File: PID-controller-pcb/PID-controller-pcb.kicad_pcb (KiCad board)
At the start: 2 copper layers, 165.4 x 86 mm, 12 parts, among them SW1 PinHeader_1x03_P2.54mm_Vertic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

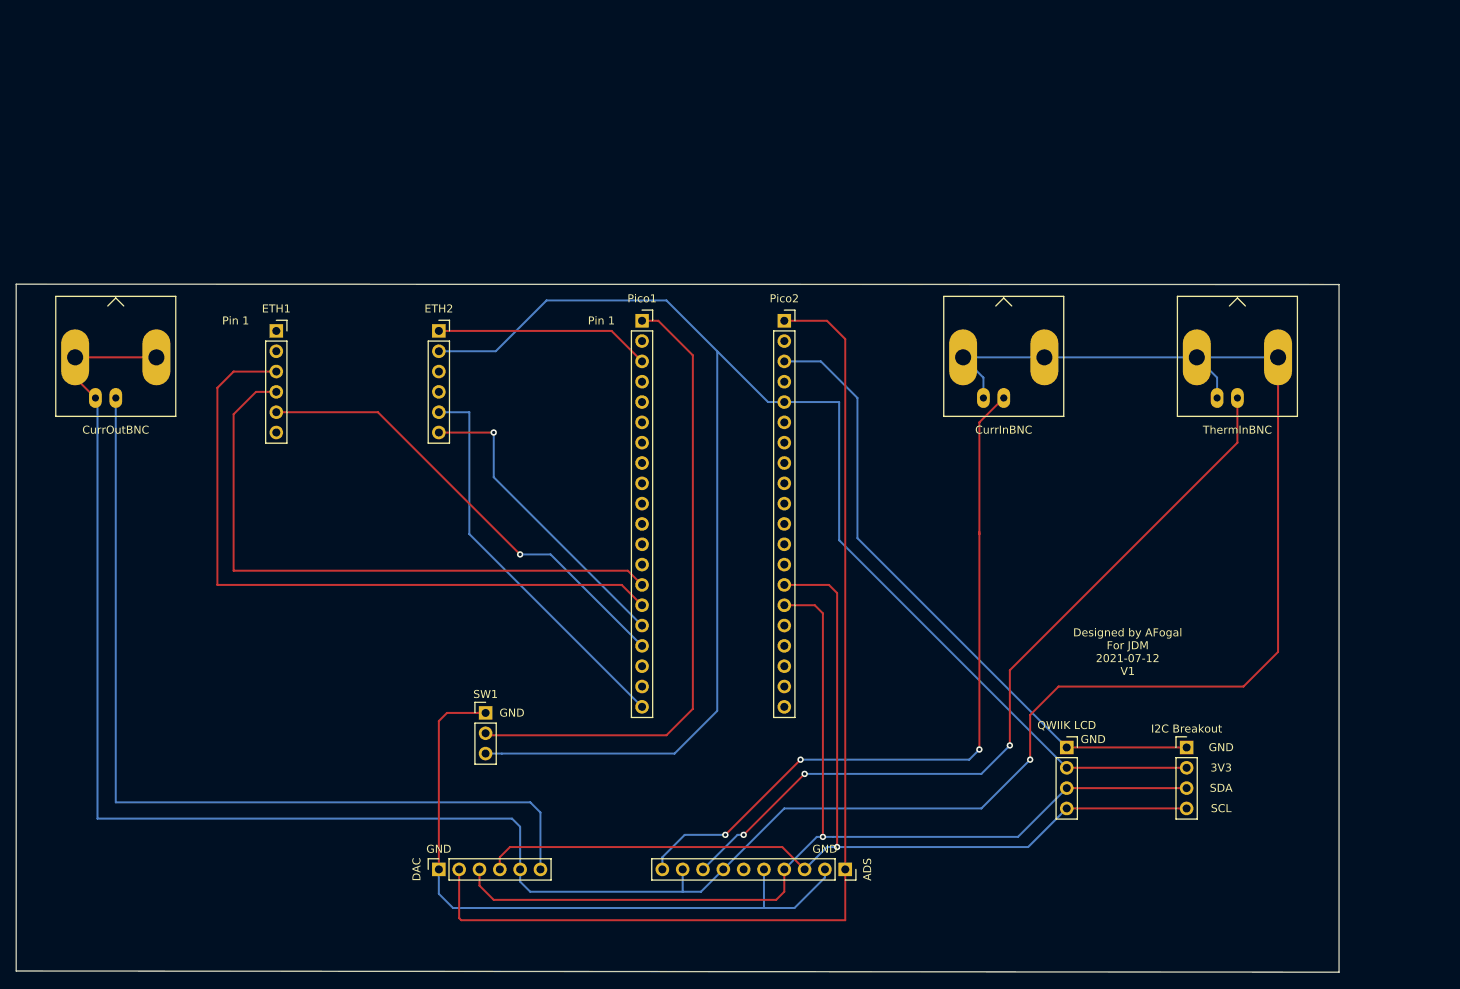
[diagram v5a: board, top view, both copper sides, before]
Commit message: added beagle spy breakout for spi and i2c, didnt route pins 4 or 6 (used for powering device) as we do not want 5V power for spi or i2c
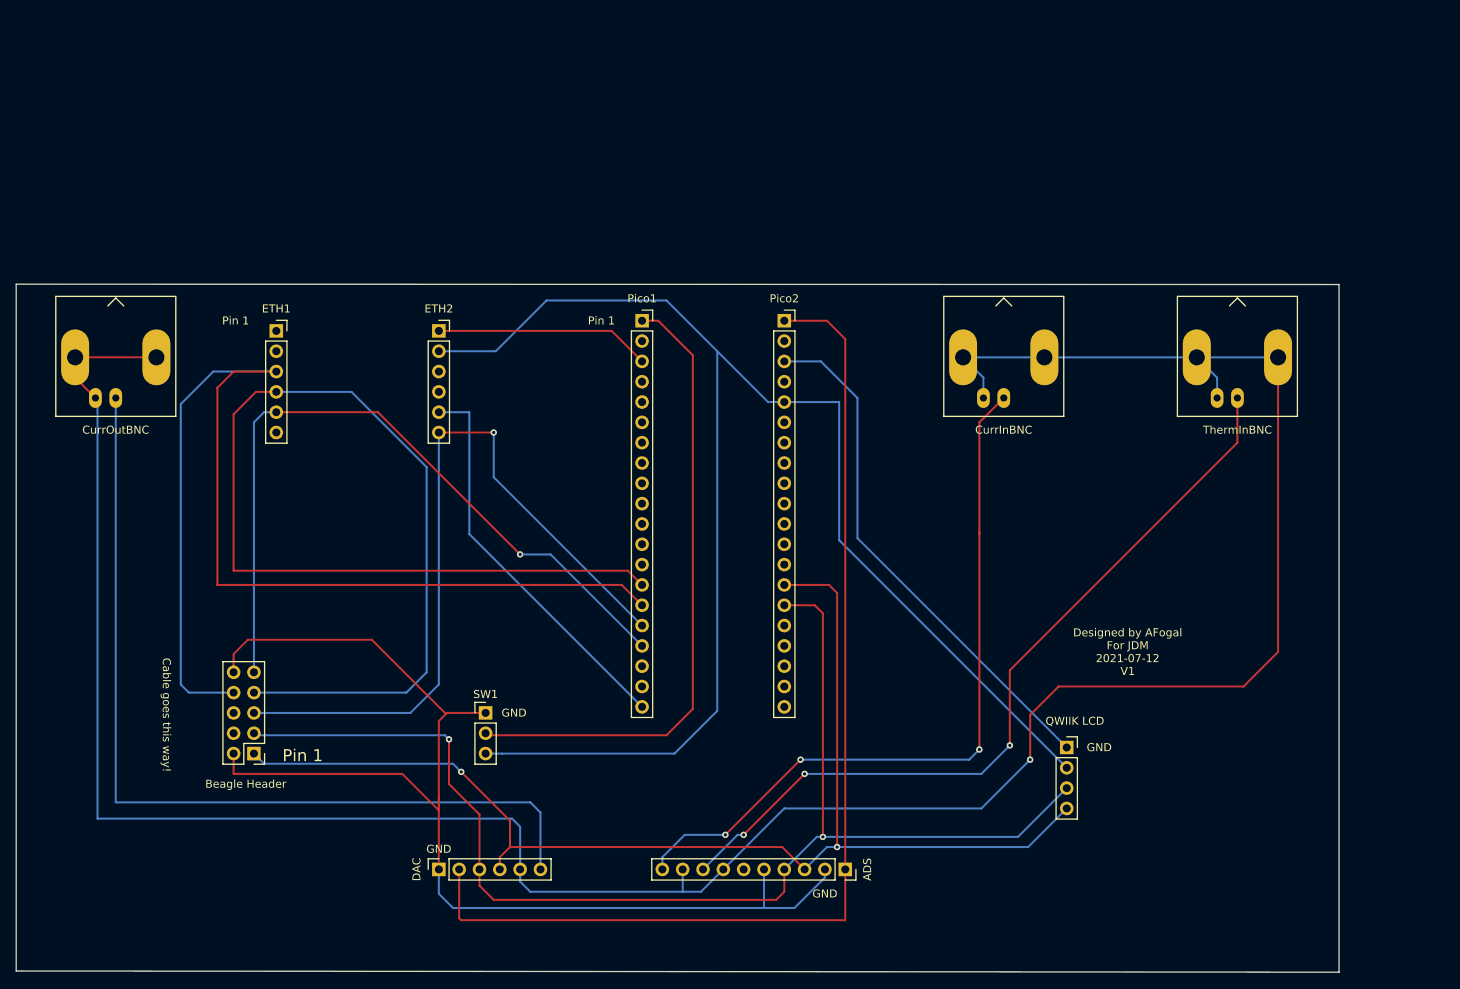
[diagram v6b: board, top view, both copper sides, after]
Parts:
- removed I2C Breakout: PinHeader_1x04_P2.54mm_Vertical, Connector_PinHeader_2.54mm:PinHeader_1x04_P2.54mm_Vertical
- added Beagle Header: PinHeader_2x05_P2.54mm_Vertical, Connector_PinHeader_2.54mm:PinHeader_2x05_P2.54mm_Vertical, F.Cu at (133.1, 103.6)
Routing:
- net (no net): track 1822.1 -> 2126.1 mm, vias 11 -> 13
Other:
- board text added: "Cable goes this way!"
- board text removed: "3V3"
- board text removed: "SCL"
- board text removed: "SDA"

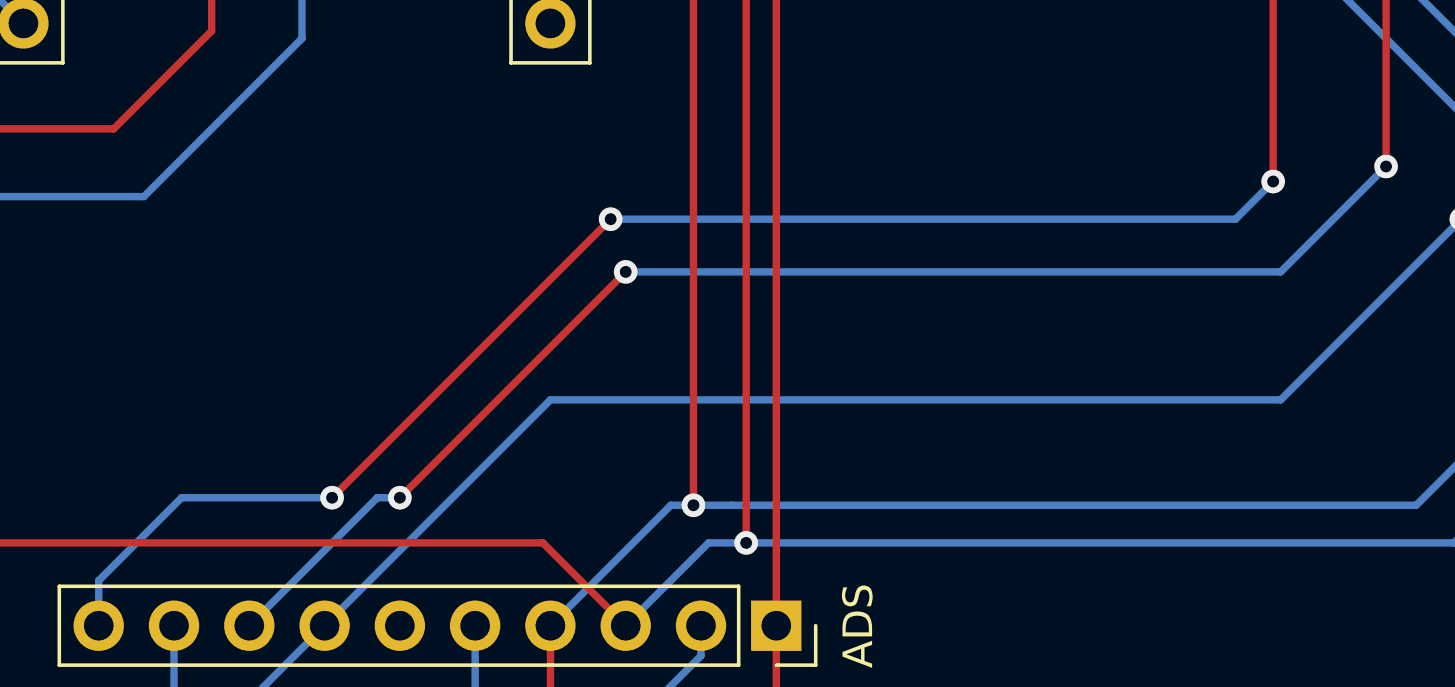
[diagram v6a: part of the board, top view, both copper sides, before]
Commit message: slightly simplified board traces
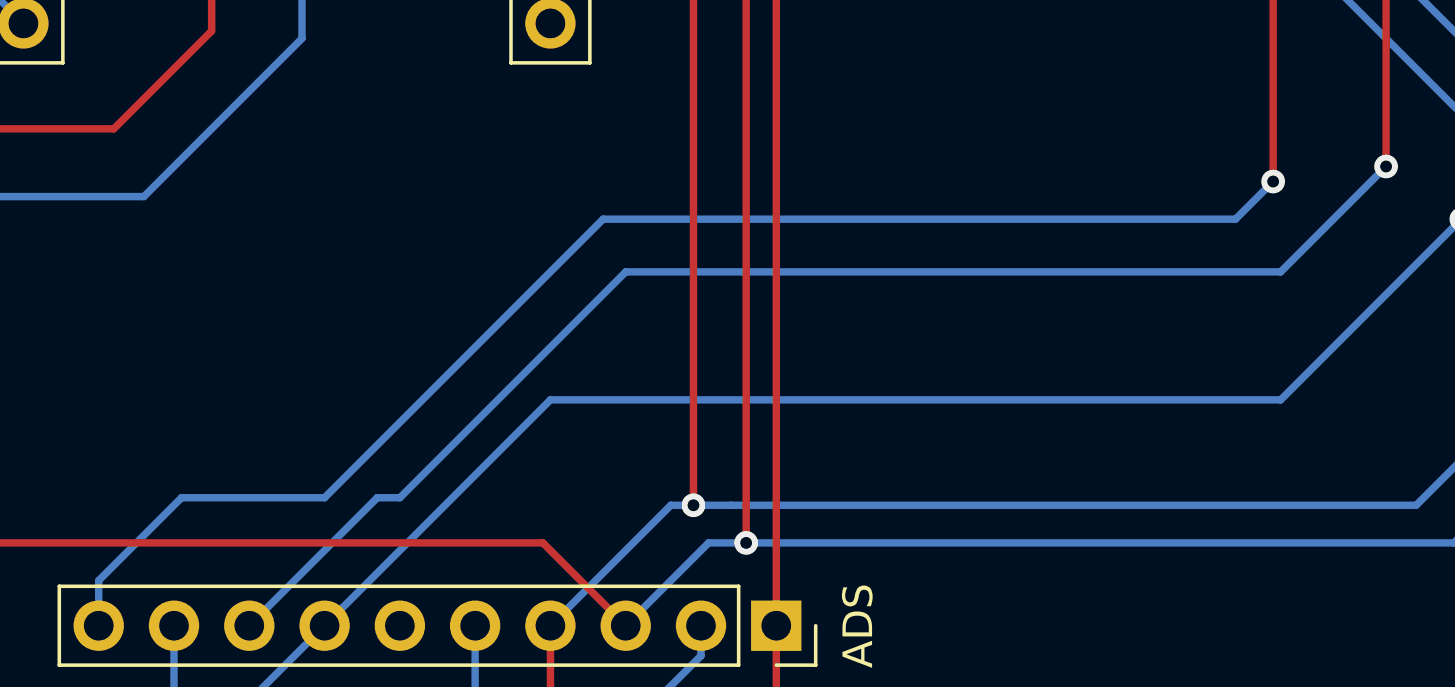
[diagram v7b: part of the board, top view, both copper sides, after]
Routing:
- net (no net): vias 13 -> 9
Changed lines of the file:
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@@
     (thickness 1.6)
     (drawings 13)
-    (tracks 195)
+    (tracks 189)
     (zones 0)
     (modules 12)
@@
   (segment (start 166.37 122.936) (end 196.85 122.936) (width 0.25) (layer B.Cu) (net 0))
   (segment (start 194.31 113.792) (end 194.31 113.792) (width 0.25) (layer B.Cu) (net 0))
-  (via (at 194.31 113.792) (size 0.8) (drill 0.4) (layers F.Cu B.Cu) (net 0))
-  (segment (start 194.31 113.792) (end 201.93 106.172) (width 0.25) (layer F.Cu) (net 0))
   (segment (start 201.93 106.172) (end 201.93 106.172) (width 0.25) (layer F.Cu) (net 0))
-  (via (at 201.93 106.172) (size 0.8) (drill 0.4) (layers F.Cu B.Cu) (net 0))
   (segment (start 227.584 102.616) (end 227.584 102.616) (width 0.25) (layer B.Cu) (net 0))
   (via (at 227.584 102.616) (size 0.8) (drill 0.4) (layers F.Cu B.Cu) (net 0))
@@
   (segment (start 184.15 118.11) (end 184.15 116.586) (width 0.25) (layer B.Cu) (net 0))
   (segment (start 184.15 116.586) (end 186.944 113.792) (width 0.25) (layer B.Cu) (net 0))
-  (segment (start 186.944 113.792) (end 192.024 113.792) (width 0.25) (layer B.Cu) (net 0))
-  (segment (start 192.024 113.792) (end 192.024 113.792) (width 0.25) (layer B.Cu) (net 0))
-  (via (at 192.024 113.792) (size 0.8) (drill 0.4) (layers F.Cu B.Cu) (net 0))
-  (segment (start 192.024 113.792) (end 201.422 104.394) (width 0.25) (layer F.Cu) (net 0))
-  (segment (start 201.422 104.394) (end 201.422 104.394) (width 0.25) (layer F.Cu) (net 0))
-  (via (at 201.422 104.394) (size 0.8) (drill 0.4) (layers F.Cu B.Cu) (net 0))
-  (segment (start 201.422 104.394) (end 222.504 104.394) (width 0.25) (layer B.Cu) (net 0))
-  (segment (start 222.504 104.394) (end 223.774 103.124) (width 0.25) (layer B.Cu) (net 0))
   (segment (start 223.774 103.124) (end 223.774 103.124) (width 0.25) (layer B.Cu) (net 0))
   (via (at 223.774 103.124) (size 0.8) (drill 0.4) (layers F.Cu B.Cu) (net 0))
@@
   (segment (start 156.21 110.744) (end 151.638 106.172) (width 0.25) (layer F.Cu) (net 0))
   (segment (start 156.21 108.966) (end 156.21 110.744) (width 0.25) (layer F.Cu) (net 0))
+  (segment (start 201.168 104.394) (end 191.77 113.792) (width 0.25) (layer B.Cu) (net 0))
+  (segment (start 222.504 104.394) (end 201.168 104.394) (width 0.25) (layer B.Cu) (net 0))
+  (segment (start 223.774 103.124) (end 222.504 104.394) (width 0.25) (layer B.Cu) (net 0))
+  (segment (start 186.944 113.792) (end 191.77 113.792) (width 0.25) (layer B.Cu) (net 0))
+  (segment (start 201.93 106.172) (end 194.31 113.792) (width 0.25) (layer B.Cu) (net 0))
 )
